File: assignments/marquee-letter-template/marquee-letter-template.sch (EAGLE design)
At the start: 19 parts, among them Q2 MMBT2222A-TP

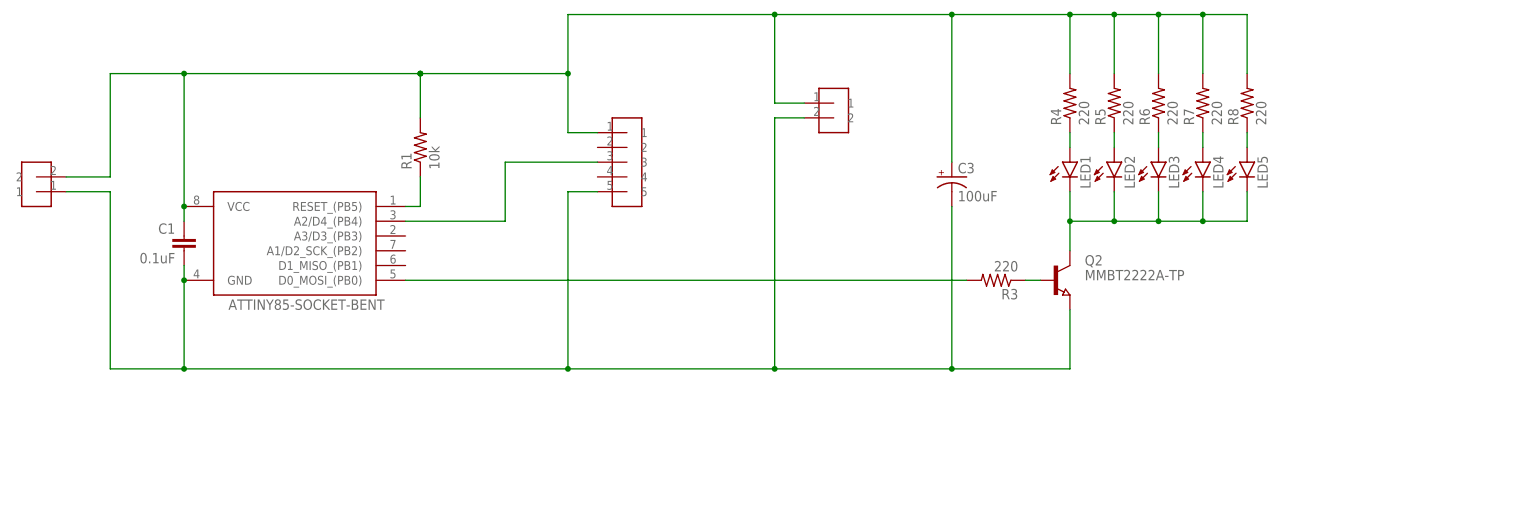
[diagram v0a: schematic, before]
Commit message: marquee template; shrinks some footprints for marquee board
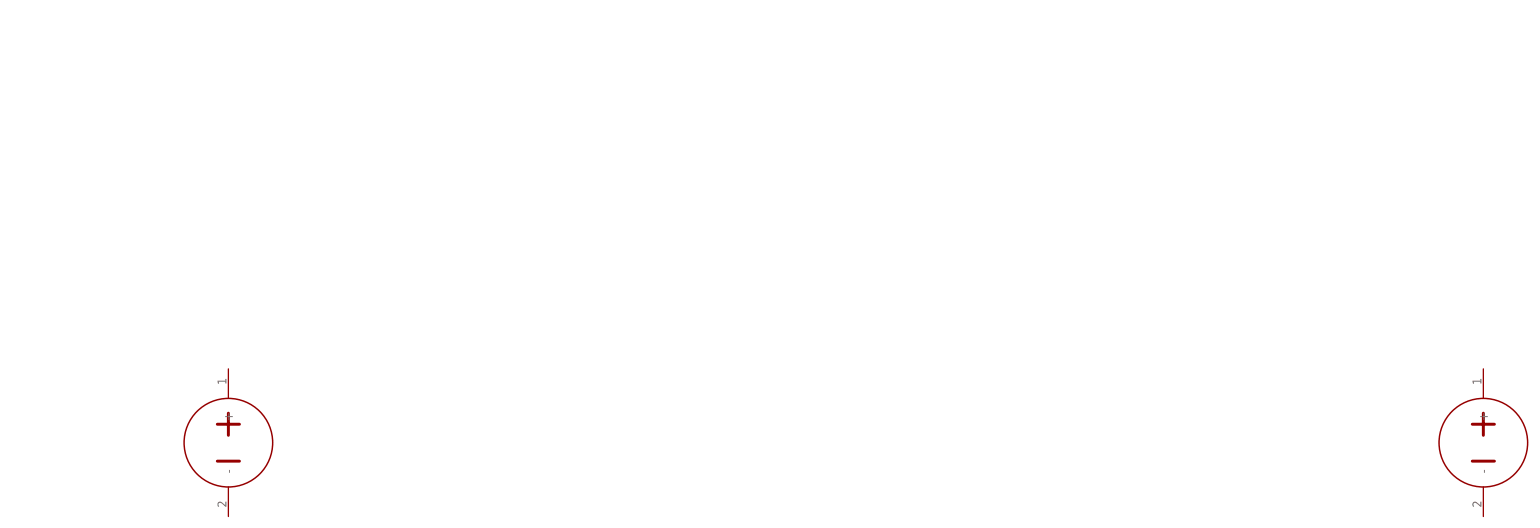
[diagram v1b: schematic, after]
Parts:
- removed C1: 0.1uF, homemade-hardware:CAP-0805
- removed C3: 100uF, homemade-hardware:CAP_POLD
- removed LED1, LED2, LED3, LED4, LED5: (no value), homemade-hardware:LED0603
- removed POTENTIOMETER: HEADER-5, homemade-hardware:HEADER-5
- removed Q2: MMBT2222A-TP, homemade-hardware:TRANSISTOR-NPN-SOT23
- removed R1: 10k, homemade-hardware:RESISTOR-0805
- removed R3: 220, homemade-hardware:RESISTOR-0805
- removed R4, R5, R6, R7, R8: 220, homemade-hardware:RESISTOR0603
- removed U$3: HEADER-2, homemade-hardware:HEADER-2
- U$1: value ATTINY85-SOCKET-BENT -> CONN_BATTERY-LIPO-HORIZ; device homemade-hardware:ATTINY85-SOCKET-BENT -> homemade-hardware:CONN_BATTERY-LIPO-HORIZ
- U$2: value HEADER-2 -> CONN_BATTERY-LIPO-HORIZ; device homemade-hardware:HEADER-2 -> homemade-hardware:CONN_BATTERY-LIPO-HORIZ
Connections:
- removed net 5V: C1.1, C3.+, POTENTIOMETER.1, R1.2, R4.2, R5.2, R6.2, R7.2, R8.2, U$1.VCC, U$2.2, U$3.1
- removed net GND: C1.2, C3.-, POTENTIOMETER.5, Q2.E, U$1.GND, U$2.1, U$3.2
- removed net N$1: LED1.A, R4.1
- removed net N$10: LED5.A, R8.1
- removed net N$12: R1.1, U$1.RESET_(PB5)
- removed net N$3: R3.2, U$1.D0_MOSI_(PB0)
- removed net N$4: LED1.C, LED2.C, LED3.C, LED4.C, LED5.C, Q2.C
- removed net N$5: Q2.B, R3.1
- removed net N$7: LED2.A, R5.1
- removed net N$8: LED3.A, R6.1
- removed net N$9: LED4.A, R7.1
- removed net SENSOR: POTENTIOMETER.3, U$1.A2/D4_(PB4)
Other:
- note removed: "5V"
- note removed: "Copy/Paste to add more LEDs --->>"
- note removed: "FYI: Not Connected (because no dot)"
- note removed: "GND"
- note removed: "Large Capacitor (for LED power surges)"
- note removed: "NPN Transistor"
- note removed: "Potentiometer (change header for different sensors)"
- note removed: "Power In"
- note removed: "Power Out (to next letter)"
